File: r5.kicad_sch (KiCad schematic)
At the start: 80 parts, among them SW10 SW_SPDT, SW60 SW_SPDT, SW70 SW_SPDT, SW80 SW_SPDT, U10 LMZ22005, U20 DRV8871DDA, U21 DRV8871DDA, U22 DRV8871DDA, U23 DRV8871DDA, U24 DRV8871DDA, U25 DRV8871DDA, U50 PI22, U51 74HC541, U60 PCA9685PW, U71 74HC540, U80 Pico, X10 Conn_01x02, X11 Conn_01x02, X12 Conn_01x02, X20 Conn_01x06, X21 Conn_01x06, X22 Conn_01x06, X23 Conn_01x06, X24 Conn_01x06, X25 Conn_01x06, X40 Conn_01x04, X90 3X3HEADER, X91 4X3HEADER, X92 SDD1309, X93 GY-BNO08X

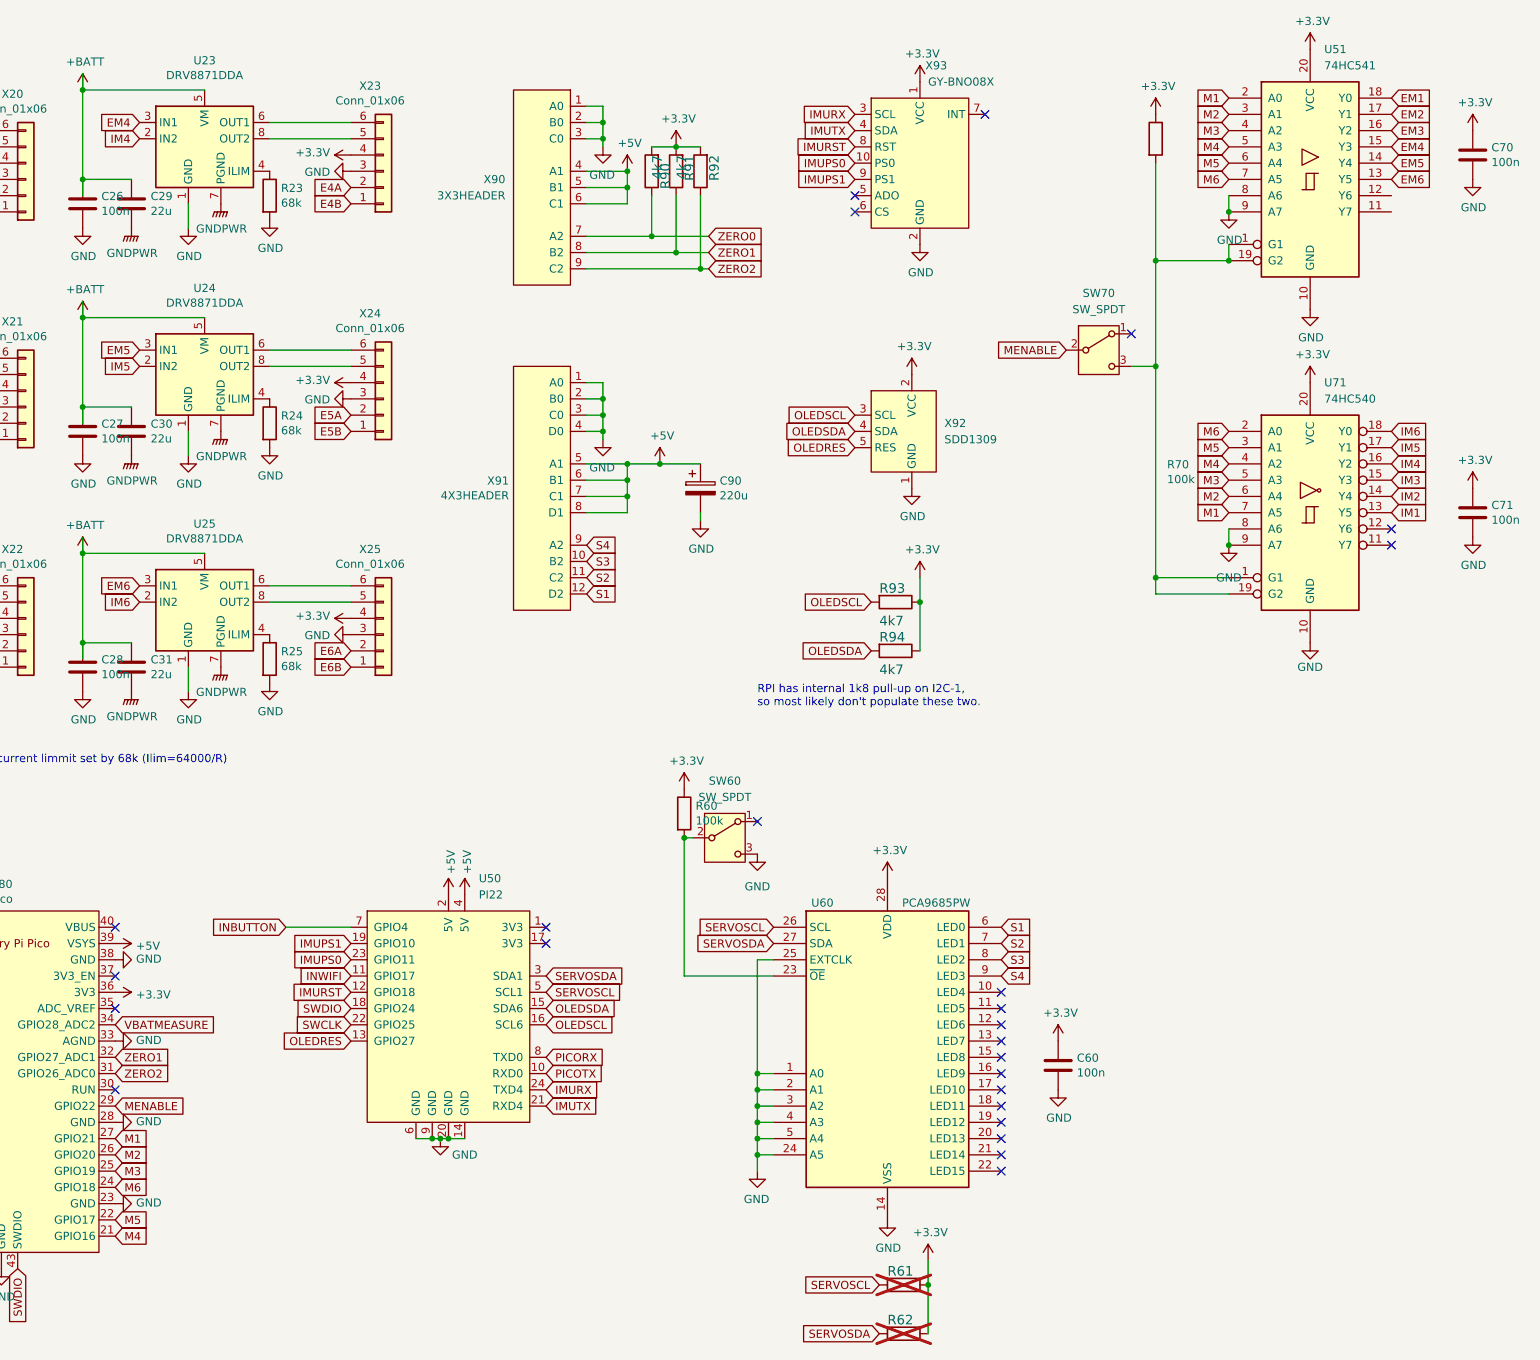
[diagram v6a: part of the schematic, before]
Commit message: use 2 inverters
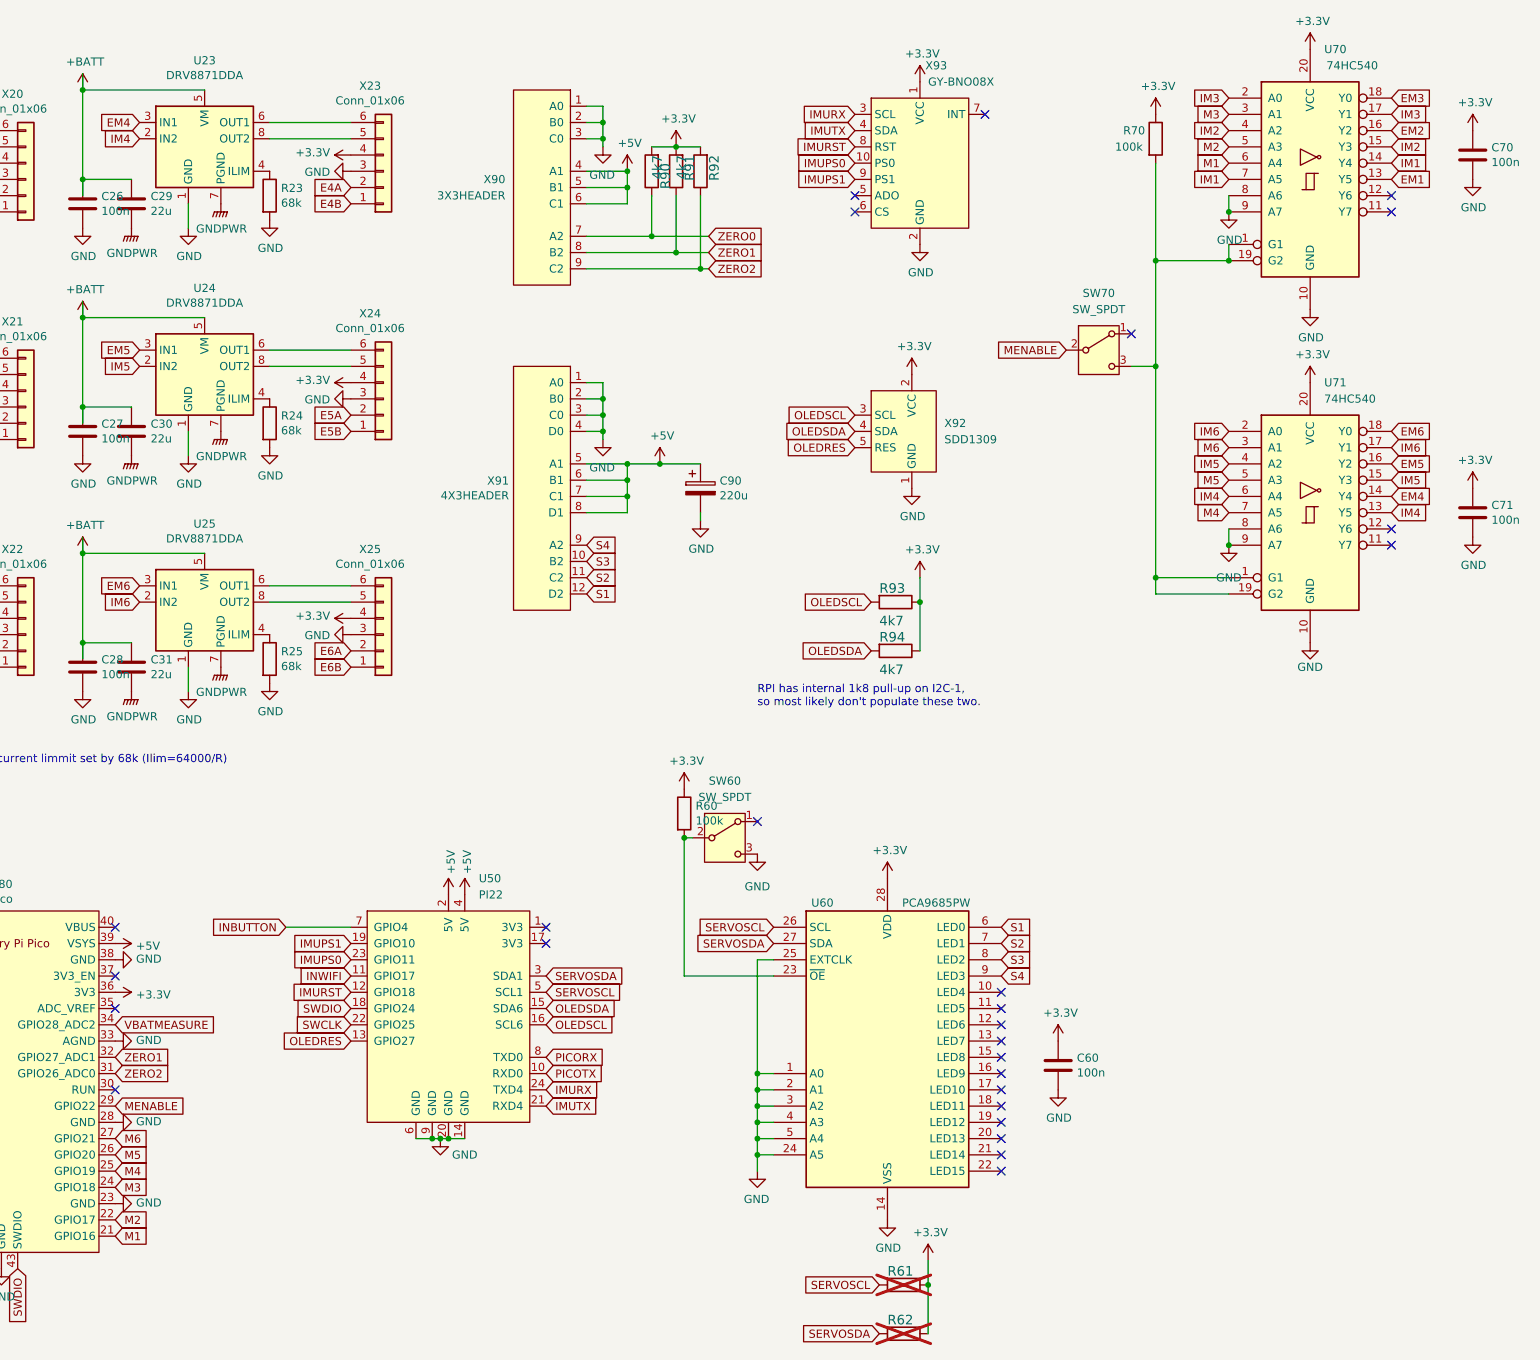
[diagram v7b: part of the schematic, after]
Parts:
- removed U51: 74HC541, Package_SO:TSSOP-20_4.4x6.5mm_P0.65mm, symbol 74xx:74LS541
- added U70: 74HC540, Package_SO:TSSOP-20_4.4x6.5mm_P0.65mm, symbol 74xx:74LS540
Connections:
- net +3.3V: now also U70.20 (VCC)
- net EM1: now also U70.13 (Y5)
- net EM2: now also U70.16 (Y2)
- net EM3: now also U70.18 (Y0)
- net EM4: now also U71.14 (Y4)
- net EM5: now also U71.16 (Y2)
- net EM6: now also U71.18 (Y0)
- net GND: now also U70.10 (GND), U70.8 (A6), U70.9 (A7)
- net IM1: now also U70.14 (Y4), U70.7 (A5); no longer U71.13 (Y5)
- net IM2: now also U70.15 (Y3), U70.4 (A2); no longer U71.14 (Y4)
- net IM3: now also U70.17 (Y1), U70.2 (A0); no longer U71.15 (Y3)
- net IM4: now also U71.13 (Y5), U71.6 (A4); no longer U71.16 (Y2)
- net IM5: now also U71.15 (Y3), U71.4 (A2); no longer U71.17 (Y1)
- net IM6: now also U71.17 (Y1), U71.2 (A0); no longer U71.18 (Y0)
- net M1: now also U80.21 (GPIO16), U70.6 (A4); no longer U71.7 (A5), U80.27 (GPIO21)
- net M2: now also U80.22 (GPIO17), U70.5 (A3); no longer U71.6 (A4), U80.26 (GPIO20)
- net M3: now also U80.24 (GPIO18), U70.3 (A1); no longer U71.5 (A3), U80.25 (GPIO19)
- net M4: now also U71.7 (A5), U80.25 (GPIO19); no longer U71.4 (A2), U80.21 (GPIO16)
- net M5: now also U71.5 (A3), U80.26 (GPIO20); no longer U71.3 (A1), U80.22 (GPIO17)
- net M6: now also U71.3 (A1), U80.27 (GPIO21); no longer U71.2 (A0), U80.24 (GPIO18)
- net at R70.2, SW70.3 (C), U71.1 (G1)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: now also U70.1 (G1), U70.19 (G2)
- no-connect marks 28 -> 30

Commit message: routing continued
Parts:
- added NT50: NetTie_2, NetTie:NetTie-2_SMD_Pad2.0mm, symbol Device:NetTie_2
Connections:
- net GND: now also NT50.1
- net GNDPWR: now also NT50.2
- net S1: now also U60.13 (LED7); no longer U60.6 (LED0)
- net S2: now also U60.12 (LED6); no longer U60.7 (LED1)
- net S3: now also U60.15 (LED8); no longer U60.8 (LED2)
- net S4: now also U60.16 (LED9); no longer U60.9 (LED3)
- net ZERO1: now also U80.31 (GPIO26_ADC0); no longer U80.32 (GPIO27_ADC1)
- net ZERO2: now also U80.32 (GPIO27_ADC1); no longer U80.31 (GPIO26_ADC0)
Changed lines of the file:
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@@
   )
   (no_connect (at 278.13 175.26))
-  (no_connect (at 349.25 193.04))
+  (no_connect (at 349.25 177.8))
   (no_connect (at 58.42 109.22))
   (no_connect (at 410.21 58.42))
-  (no_connect (at 349.25 190.5))
+  (no_connect (at 349.25 172.72))
   (no_connect (at 210.82 185.42))
   (no_connect (at 349.25 200.66))
@@
   (no_connect (at 326.39 60.96))
   (no_connect (at 410.21 60.96))
-  (no_connect (at 349.25 187.96))
+  (no_connect (at 349.25 175.26))
   (no_connect (at 349.25 205.74))
   (no_connect (at 410.21 113.03))
@@
   (no_connect (at 45.72 107.95))
   (no_connect (at 210.82 198.12))
-  (no_connect (at 349.25 195.58))
+  (no_connect (at 349.25 180.34))
   (no_connect (at 349.25 210.82))
   (no_connect (at 326.39 58.42))
@@
     (stroke (width 0) (type default))
   )
+  (wire (pts (xy 97.79 62.23) (xy 99.06 62.23))
+    (stroke (width 0) (type default))
+  )
   (wire (pts (xy 294.64 50.8) (xy 298.45 50.8))
     (stroke (width 0) (type default))
@@
     (stroke (width 0) (type default))
   )
+  (wire (pts (xy 97.79 66.04) (xy 97.79 62.23))
+    (stroke (width 0) (type default))
+  )
   (wire (pts (xy 149.86 78.74) (xy 149.86 92.71))
     (stroke (width 0) (type default))
@@
     (stroke (width 0) (type default))
   )
+  (wire (pts (xy 104.14 62.23) (xy 106.68 62.23))
+    (stroke (width 0) (type default))
+  )
   (wire (pts (xy 284.48 67.31) (xy 298.45 67.31))
     (stroke (width 0) (type default))
@@
     (stroke (width 0) (type default))
   )
+  (wire (pts (xy 106.68 62.23) (xy 106.68 66.04))
+    (stroke (width 0) (type default))
+  )
   (wire (pts (xy 290.83 102.87) (xy 290.83 100.33))
     (stroke (width 0) (type default))
@@
     )
   )
-  (global_label "S4" (shape input) (at 349.25 180.34 0)
+  (global_label "S4" (shape input) (at 349.25 195.58 0)
     (effects (font (size 1.27 1.27)) (justify left))
-    (property "Intersheetrefs" "${INTERSHEET_REFS}" (at 349.25 180.34 0)
+    (property "Intersheetrefs" "${INTERSHEET_REFS}" (at 349.25 195.58 0)
       (effects (font (size 1.27 1.27)) hide)
     )
@@
     )
   )
-  (global_label "ZERO2" (shape input) (at 210.82 195.58 0) (fields_autoplaced)
+  (global_label "ZERO2" (shape input) (at 210.82 193.04 0) (fields_autoplaced)
     (effects (font (size 1.27 1.27)) (justify left))
-    (property "Intersheetrefs" "${INTERSHEET_REFS}" (at 219.3195 195.58 0)
+    (property "Intersheetrefs" "${INTERSHEET_REFS}" (at 219.3195 193.04 0)
       (effects (font (size 1.27 1.27)) (justify left) hide)
     )
@@
     )
   )
-  (global_label "S1" (shape input) (at 349.25 172.72 0)
+  (global_label "S1" (shape input) (at 349.25 190.5 0)
     (effects (font (size 1.27 1.27)) (justify left))
-    (property "Intersheetrefs" "${INTERSHEET_REFS}" (at 349.25 172.72 0)
+    (property "Intersheetrefs" "${INTERSHEET_REFS}" (at 349.25 190.5 0)
       (effects (font (size 1.27 1.27)) hide)
     )
@@
     )
   )
-  (global_label "ZERO1" (shape input) (at 210.82 193.04 0) (fields_autoplaced)
+  (global_label "ZERO1" (shape input) (at 210.82 195.58 0) (fields_autoplaced)
     (effects (font (size 1.27 1.27)) (justify left))
-    (property "Intersheetrefs" "${INTERSHEET_REFS}" (at 219.3195 193.04 0)
+    (property "Intersheetrefs" "${INTERSHEET_REFS}" (at 219.3195 195.58 0)
       (effects (font (size 1.27 1.27)) (justify left) hide)
     )
   )
-  (global_label "S2" (shape input) (at 349.25 175.26 0)
+  (global_label "S2" (shape input) (at 349.25 187.96 0)
     (effects (font (size 1.27 1.27)) (justify left))
-    (property "Intersheetrefs" "${INTERSHEET_REFS}" (at 349.25 175.26 0)
+    (property "Intersheetrefs" "${INTERSHEET_REFS}" (at 349.25 187.96 0)
       (effects (font (size 1.27 1.27)) hide)
     )
   )
-  (global_label "S3" (shape input) (at 349.25 177.8 0)
+  (global_label "S3" (shape input) (at 349.25 193.04 0)
     (effects (font (size 1.27 1.27)) (justify left))
-    (property "Intersheetrefs" "${INTERSHEET_REFS}" (at 349.25 177.8 0)
+    (property "Intersheetrefs" "${INTERSHEET_REFS}" (at 349.25 193.04 0)
       (effects (font (size 1.27 1.27)) hide)
     )
@@
     )
   )
-  (symbol (lib_id "power:GNDPWR") (at 104.14 66.04 0) (unit 1)
+  (symbol (lib_id "power:GNDPWR") (at 106.68 66.04 0) (unit 1)
     (in_bom yes) (on_board yes) (dnp no)
-    (property "Reference" "#PWR0218" (at 104.14 71.12 0)
+    (property "Reference" "#PWR0218" (at 106.68 71.12 0)
       (effects (font (size 1.27 1.27)) hide)
     )
-    (property "Value" "GNDPWR" (at 104.2416 69.9516 0)
+    (property "Value" "GNDPWR" (at 106.7816 69.9516 0)
       (effects (font (size 1.27 1.27)))
     )
-    (property "Footprint" "" (at 104.14 67.31 0)
+    (property "Footprint" "" (at 106.68 67.31 0)
       (effects (font (size 1.27 1.27)) hide)
     )
-    (property "Datasheet" "" (at 104.14 67.31 0)
+    (property "Datasheet" "" (at 106.68 67.31 0)
       (effects (font (size 1.27 1.27)) hide)
     )
@@
         )
       )
+    )
+  )
+  (symbol (lib_id "Device:NetTie_2") (at 101.6 62.23 0) (unit 1)
+    (in_bom no) (on_board yes) (dnp no) (fields_autoplaced)
+    (property "Reference" "NT50" (at 101.6 57.15 0)
+      (effects (font (size 1.27 1.27)))
+    )
+    (property "Value" "NetTie_2" (at 101.6 59.69 0)
+      (effects (font (size 1.27 1.27)))
+    )
+    (property "Footprint" "NetTie:NetTie-2_SMD_Pad2.0mm" (at 101.6 62.23 0)
+      (effects (font (size 1.27 1.27)) hide)
+    )
+    (property "Datasheet" "~" (at 101.6 62.23 0)
+      (effects (font (size 1.27 1.27)) hide)
+    )
+    (pin "2")
+    (pin "1")
+    (instances
+      (project "r5"
+        (path "/7141c11d-0c81-438d-ad8c-6c0ffa292856"
+          (reference "NT50") (unit 1)
+        )
+      )
